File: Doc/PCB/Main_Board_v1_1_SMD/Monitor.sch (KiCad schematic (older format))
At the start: 60 parts, among them J1 TE_3.5mm_Screwless_P2, J2 TE_3.5mm_Screwless_P2, J3 UART_M, J4 Conn_01x08, J5 BUZZER, J6 I2C Interface LCD_M, Q1 FDT1600N10ALZ, Q4 BSR19A, SW1 MUTE, SW2 HIST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

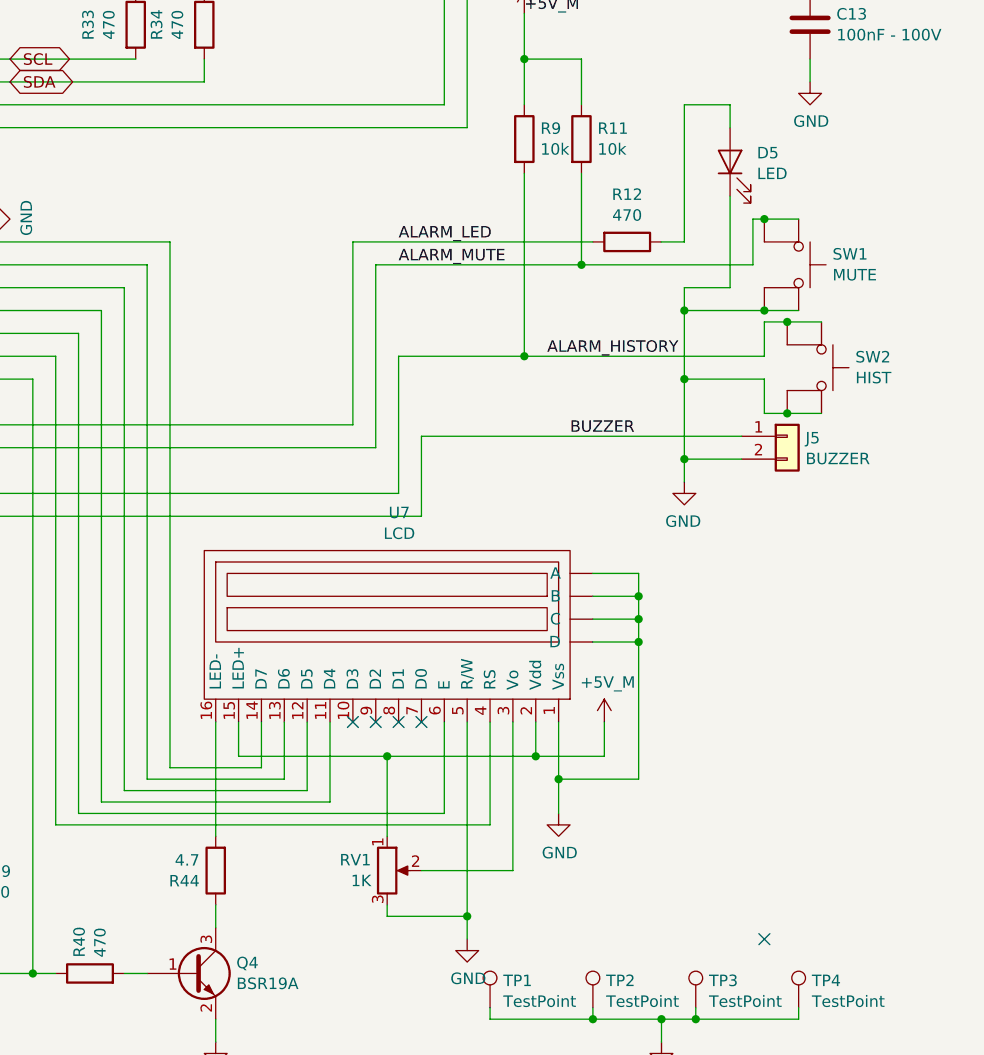
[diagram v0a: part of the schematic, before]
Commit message: First tests with artificial lung. 70 cases. New PCB THT fixing mounting issues
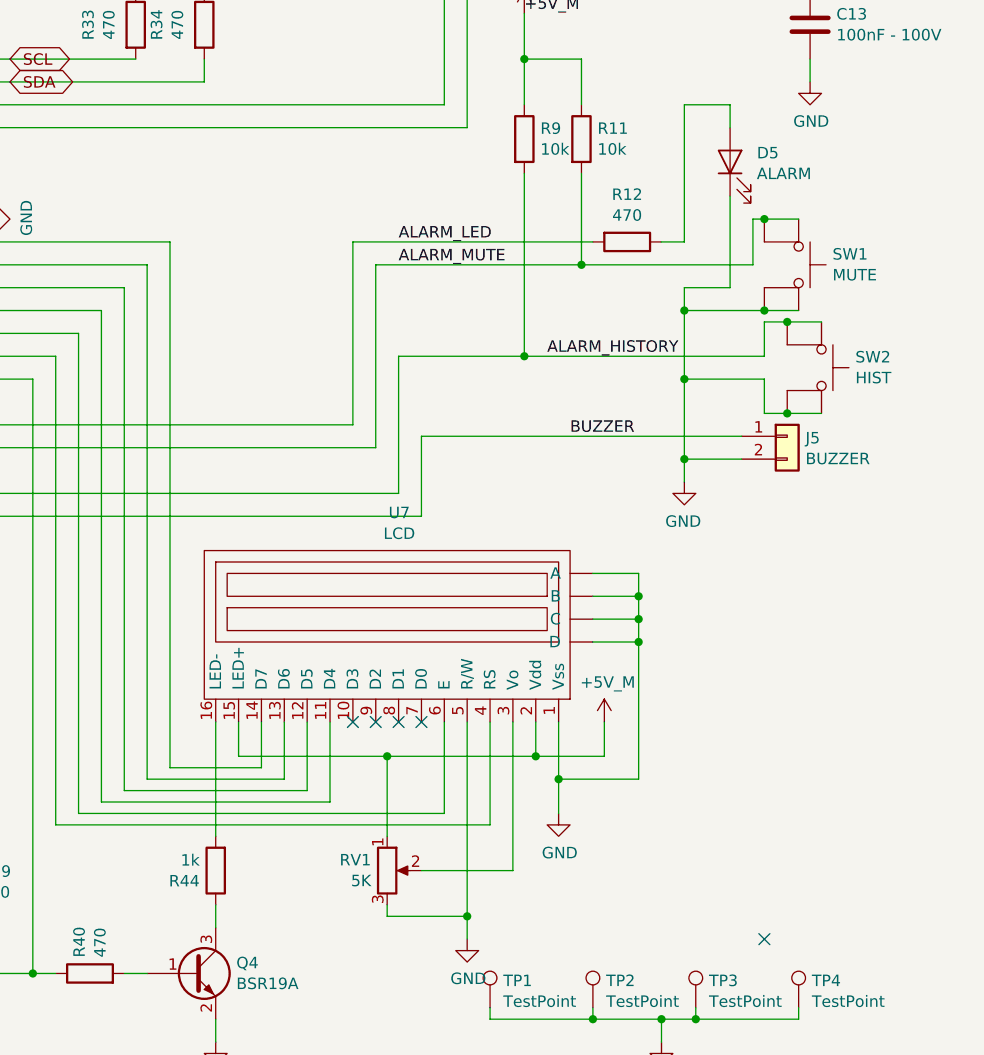
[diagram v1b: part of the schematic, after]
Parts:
- D5: value LED -> ALARM
- R44: value 4.7 -> 1k
- RV1: value 1K -> 5K; footprint Ventilator:Potentiometer_409HA -> Potentiometer_SMD:Potentiometer_Vishay_TS53YJ_Vertical
- U1: footprint Package_SO:SOIC-8-1EP_3.9x4.9mm_P1.27mm_EP2.29x3mm_ThermalVias -> Package_SO:SOIC-8-1EP_3.9x4.9mm_P1.27mm_EP2.41x3.3mm
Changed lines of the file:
@@
 F 1 "XPRESS-40" H 5875 3174 50  0000 C CNN
 F 2 "Package_DFN_QFN:UQFN-40-1EP_5x5mm_P0.4mm_EP3.8x3.8mm_ThermalVias" H 6200 2150 50  0001 C CNN
-F 3 "https://es.rs-online.com/web/p/kits-de-desarrollo-de-procesador-y-microcontrolador/1744238/" H 6200 2150 50  0001 C CNN
+F 3 "https://es.rs-online.com/web/p/microcontroladores/1717862/" H 6200 2150 50  0001 C CNN
 	1    6200 2150
 	1    0    0    -1
@@
 F 1 "LCD" H 9003 5724 50  0000 C CNN
 F 2 "Ventilator:LCD_2x16" H 8800 4900 50  0001 C CNN
-F 3 "" H 8800 4900 50  0001 C CNN
+F 3 "https://es.rs-online.com/web/p/displays-monocromos-lcd/1631922/" H 8800 4900 50  0001 C CNN
 	1    8800 4900
 	1    0    0    -1
@@
 F 1 "1uF" H 5015 7055 50  0000 L CNN
 F 2 "Capacitor_SMD:C_1206_3216Metric_Pad1.42x1.75mm_HandSolder" H 4938 6950 50  0001 C CNN
-F 3 "https://es.rs-online.com/web/p/mlccs-condensadores-ceramicos-multicapa/1364396/" H 4900 7100 50  0001 C CNN
+F 3 "Capacitor_SMD:C_1206_3216Metric_Pad1.42x1.75mm_HandSolder" H 4900 7100 50  0001 C CNN
 	1    4900 7100
 	-1   0    0    -1
@@
 F 1 "1uF" H 1165 4505 50  0000 L CNN
 F 2 "Capacitor_SMD:C_1206_3216Metric_Pad1.42x1.75mm_HandSolder" H 1088 4400 50  0001 C CNN
-F 3 "https://es.rs-online.com/web/p/mlccs-condensadores-ceramicos-multicapa/1364396/" H 1050 4550 50  0001 C CNN
+F 3 "Capacitor_SMD:C_1206_3216Metric_Pad1.42x1.75mm_HandSolder" H 1050 4550 50  0001 C CNN
 	1    1050 4550
 	-1   0    0    -1
@@
 F 1 "1uF" H 2165 4055 50  0000 L CNN
 F 2 "Capacitor_SMD:C_1206_3216Metric_Pad1.42x1.75mm_HandSolder" H 2088 3950 50  0001 C CNN
-F 3 "https://es.rs-online.com/web/p/mlccs-condensadores-ceramicos-multicapa/1364396/" H 2050 4100 50  0001 C CNN
+F 3 "Capacitor_SMD:C_1206_3216Metric_Pad1.42x1.75mm_HandSolder" H 2050 4100 50  0001 C CNN
 	1    2050 4100
 	-1   0    0    -1
@@
 F 0 "U1" H 3958 6546 50  0000 L CNN
 F 1 "LM358" H 3958 6455 50  0000 L CNN
-F 2 "Package_SO:SOIC-8-1EP_3.9x4.9mm_P1.27mm_EP2.29x3mm_ThermalVias" H 4000 6500 50  0001 C CNN
+F 2 "Package_SO:SOIC-8-1EP_3.9x4.9mm_P1.27mm_EP2.41x3.3mm" H 4000 6500 50  0001 C CNN
 F 3 "https://es.rs-online.com/web/p/amplificadores-operacionales/1787509/" H 4000 6500 50  0001 C CNN
 	3    4000 6500
@@
 F 1 "1uF" H 1665 6305 50  0000 L CNN
 F 2 "Capacitor_SMD:C_1206_3216Metric_Pad1.42x1.75mm_HandSolder" H 1588 6200 50  0001 C CNN
-F 3 "https://es.rs-online.com/web/p/mlccs-condensadores-ceramicos-multicapa/1364396/" H 1550 6350 50  0001 C CNN
+F 3 "Capacitor_SMD:C_1206_3216Metric_Pad1.42x1.75mm_HandSolder" H 1550 6350 50  0001 C CNN
 	1    1550 6350
 	1    0    0    -1
@@
 F 0 "U1" H 2250 6767 50  0000 C CNN
 F 1 "LM358" H 2250 6676 50  0000 C CNN
-F 2 "Package_SO:SOIC-8-1EP_3.9x4.9mm_P1.27mm_EP2.29x3mm_ThermalVias" H 2250 6400 50  0001 C CNN
+F 2 "Package_SO:SOIC-8-1EP_3.9x4.9mm_P1.27mm_EP2.41x3.3mm" H 2250 6400 50  0001 C CNN
 F 3 "https://es.rs-online.com/web/p/amplificadores-operacionales/1787509/" H 2250 6400 50  0001 C CNN
 	2    2250 6400
@@
 F 0 "U1" H 3150 6867 50  0000 C CNN
 F 1 "LM358" H 3150 6776 50  0000 C CNN
-F 2 "Package_SO:SOIC-8-1EP_3.9x4.9mm_P1.27mm_EP2.29x3mm_ThermalVias" H 3150 6500 50  0001 C CNN
+F 2 "Package_SO:SOIC-8-1EP_3.9x4.9mm_P1.27mm_EP2.41x3.3mm" H 3150 6500 50  0001 C CNN
 F 3 "https://es.rs-online.com/web/p/amplificadores-operacionales/1787509/" H 3150 6500 50  0001 C CNN
 	1    3150 6500
@@
 F 1 "1uF" H 1865 2805 50  0000 L CNN
 F 2 "Capacitor_SMD:C_1206_3216Metric_Pad1.42x1.75mm_HandSolder" H 1788 2700 50  0001 C CNN
-F 3 "https://es.rs-online.com/web/p/mlccs-condensadores-ceramicos-multicapa/1364396/" H 1750 2850 50  0001 C CNN
+F 3 "Capacitor_SMD:C_1206_3216Metric_Pad1.42x1.75mm_HandSolder" H 1750 2850 50  0001 C CNN
 	1    1750 2850
 	1    0    0    -1
@@
 F 1 "1uF" H 2815 3755 50  0000 L CNN
 F 2 "Capacitor_SMD:C_1206_3216Metric_Pad1.42x1.75mm_HandSolder" H 2738 3650 50  0001 C CNN
-F 3 "https://es.rs-online.com/web/p/mlccs-condensadores-ceramicos-multicapa/1364396/" H 2700 3800 50  0001 C CNN
+F 3 "Capacitor_SMD:C_1206_3216Metric_Pad1.42x1.75mm_HandSolder" H 2700 3800 50  0001 C CNN
 	1    2700 3800
 	1    0    0    -1
@@
 P 8950 5550
 F 0 "RV1" H 8880 5596 50  0000 R CNN
-F 1 "1K" H 8880 5505 50  0000 R CNN
-F 2 "Ventilator:Potentiometer_409HA" H 8950 5550 50  0001 C CNN
-F 3 "https://es.rs-online.com/web/p/resistencias-variables/6524546/" H 8950 5550 50  0001 C CNN
+F 1 "5K" H 8880 5505 50  0000 R CNN
+F 2 "Potentiometer_SMD:Potentiometer_Vishay_TS53YJ_Vertical" H 8950 5550 50  0001 C CNN
+F 3 "https://es.rs-online.com/web/p/resistencias-variables/1679441/" H 8950 5550 50  0001 C CNN
 	1    8950 5550
 	1    0    0    -1
@@
 F 1 "LM78M05_TO252" H 2650 1101 50  0000 C CNN
 F 2 "Package_TO_SOT_SMD:TO-252-2" H 2650 1175 50  0001 C CIN
-F 3 "http://www.fairchildsemi.com/ds/LM/LM78M05.pdf" H 2650 900 50  0001 C CNN
+F 3 "https://es.rs-online.com/web/p/reguladores-de-tension-lineal/8578558/" H 2650 900 50  0001 C CNN
 	1    2650 950
 	1    0    0    -1
@@
 F 1 "BSR19A" H 8290 5955 50  0000 L CNN
 F 2 "Package_TO_SOT_SMD:TSOT-23" H 8300 5925 50  0001 L CIN
-F 3 "https://www.fairchildsemi.com/datasheets/2N/2N3904.pdf" H 8100 6000 50  0001 L CNN
+F 3 "https://es.rs-online.com/web/p/transistores-bipolares-y-bjt/1821856/" H 8100 6000 50  0001 L CNN
 	1    8100 6000
 	1    0    0    -1
@@
 AR Path="/5E9337AC/5EB637BA" Ref="R44"  Part="1"
 F 0 "R44" H 8270 5596 50  0000 L CNN
-F 1 "4.7" H 8270 5505 50  0000 L CNN
+F 1 "1k" H 8270 5505 50  0000 L CNN
 F 2 "Resistor_SMD:R_0603_1608Metric_Pad1.05x0.95mm_HandSolder" V 8130 5550 50  0001 C CNN
 F 3 "~" H 8200 5550 50  0001 C CNN
@@
 P 10450 2450
 F 0 "D5" V 10489 2333 50  0000 R CNN
-F 1 "LED" V 10398 2333 50  0000 R CNN
+F 1 "ALARM" V 10398 2333 50  0000 R CNN
 F 2 "LED_THT:LED_D3.0mm" H 10450 2450 50  0001 C CNN
 F 3 "~" H 10450 2450 50  0001 C CNN

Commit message: New SMD PCB
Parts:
- U3: footprint Package_DFN_QFN:UQFN-40-1EP_5x5mm_P0.4mm_EP3.8x3.8mm_ThermalVias -> Package_DFN_QFN:UQFN-40-1EP_5x5mm_P0.4mm_EP3.8x3.8mm
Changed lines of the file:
@@
 F 0 "U3" H 5875 3265 50  0000 C CNN
 F 1 "XPRESS-40" H 5875 3174 50  0000 C CNN
-F 2 "Package_DFN_QFN:UQFN-40-1EP_5x5mm_P0.4mm_EP3.8x3.8mm_ThermalVias" H 6200 2150 50  0001 C CNN
+F 2 "Package_DFN_QFN:UQFN-40-1EP_5x5mm_P0.4mm_EP3.8x3.8mm" H 6200 2150 50  0001 C CNN
 F 3 "https://es.rs-online.com/web/p/microcontroladores/1717862/" H 6200 2150 50  0001 C CNN
 	1    6200 2150
